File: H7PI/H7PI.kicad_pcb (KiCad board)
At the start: 4 copper layers, 65 x 30 mm, 52 parts, among them J1 XKTF-015-N, J10 DNP, J2 Header_2x10, J3 microUSB, J4 AFC07-S24ECA-00, J5 Header_2x20, J6 microUSB, J7 Header_1x2, J8 Header_1x1, J9 Header_1x1, Q1 CJ2101, Q2 CJ2102, U2 MT1470, U3 STM32H750VBT6, U4 W25Q64JVSSIQ, U5 W25Q64JVSSIQ

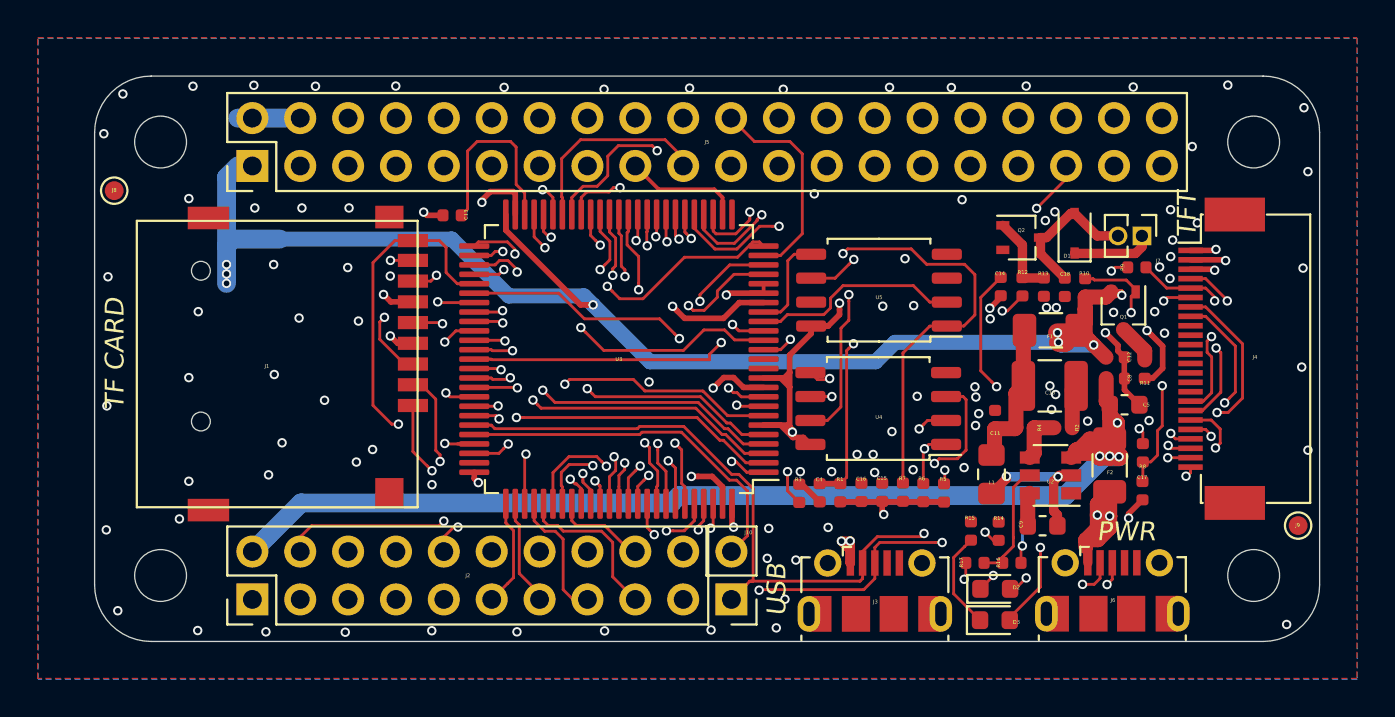
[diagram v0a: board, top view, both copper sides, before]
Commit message: v1.0开发起点 1. 不再使用树莓派外型 2. 使用Type C USB接口 3. 不再板载LCD接口 4. 板载PSRAM,QSPI FLASH,SPI FLASH 5. 保留TF卡接口
Signed-off-by: fuhua-chen <fuhua-chen@outlook.com>
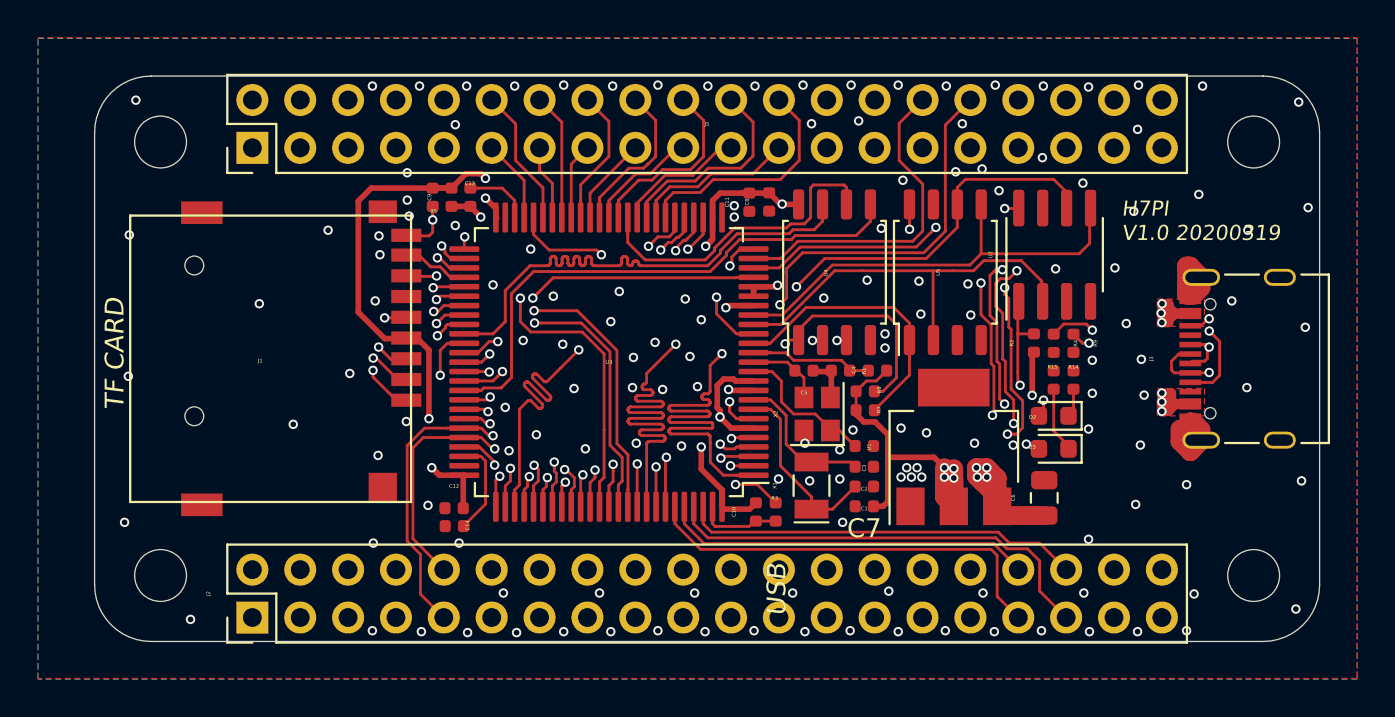
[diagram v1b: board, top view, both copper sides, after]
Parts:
- removed C15, C16, C17, C18: 100nF, C_0402_1005Metric
- removed D1: 1N5819WS, D_SOD-323
- removed F1, F2: 0458002.DR, Fuse_1206_3216Metric
- removed J10: DNP, PinHeader_1x02_P2.54mm_Vertical
- removed J4: AFC07-S24ECA-00, Connector_FPC_JS_AFC07-S24ECA-00_1x24-1MP_P0.5mm_UpSideContact
- removed J6: microUSB, USB_Micro-B_Molex-105017-0001
- removed J7: Header_1x2, Connector_PinHeader_1.27mm:PinHeader_1x02_P1.27mm_Vertical
- removed J8, J9: Header_1x1, TestPoint:TestPoint_Pad_D1.0mm
- removed L1: CIGT201610LH2R2MNE, L_0805_2012Metric_Pad1.15x1.40mm_HandSolder
- removed Q1: CJ2101, SOT-323_SC-70
- removed Q2: CJ2102, SOT-323_SC-70
- removed R10, R13, R8: 10k, R_0402_1005Metric
- removed R11: 4.7, R_0402_1005Metric
- removed R12: 1k, R_0402_1005Metric
- removed R16: 100k, R_0402_1005Metric
- removed R17: 33k, R_0402_1005Metric
- added C1: 12pF, C_0402_1005Metric, F.Cu at (170.8, 81.8)
- added C2: 12pF, C_0402_1005Metric, F.Cu at (170.8, 80.7)
- added C3: 8pF, C_0402_1005Metric, F.Cu at (170.8, 79.6)
- added C6: 22uF, Capacitor_SMD:C_0805_2012Metric, F.Cu at (180.4, 82.4)
- added C7: 10uF, C_0402_1005Metric, F.Cu at (170.8, 82.8)
- added U1: AMS1117-3.3, SOT-223, F.Cu at (175.6, 79.7)
- added X1: 32.768kHz, Crystal_SMD_EuroQuartz_EQ161-2Pin_3.2x1.5mm, F.Cu at (168.0, 81.7)
- added X2: 32MHz, Crystal:Crystal_SMD_2520-4Pin_2.5x2.0mm, F.Cu at (168.3, 77.9)
- C10: value 100uF/10V -> 100nF; footprint C_1210_3225Metric -> C_0402_1005Metric
- C5: value 1uF -> 8pF; footprint C_0603_1608Metric -> C_0402_1005Metric
- C9: value 1uF -> 100nF; footprint C_0603_1608Metric -> C_0402_1005Metric
- J2: value Header_2x10 -> Header_2x20; footprint PinHeader_2x10_P2.54mm_Vertical -> PinHeader_2x20_P2.54mm_Vertical
- J3: value microUSB -> USBC_16P_4MP; footprint USB_Micro-B_Molex-105017-0001 -> USB_C_Receptacle_Palconn_UTC16-G
- R2: value 33k -> 10k
- R4: value 100k -> 4.7k
- R9: value 10k -> 4.7k
- U2: value MT1470 -> LY68L6400SLIT; footprint SOT-23-6 -> SOIC-8_3.9x4.9mm_P1.27mm
- moved C12 36.0 mm to (149.1, 82.9), turned to 0 degrees
- moved C9 35.9 mm to (148.9, 66.4), turned to 90 degrees
- moved C14 31.7 mm to (149.1, 83.9), turned to 180 degrees
- moved R5 31.3 mm to (147.9, 66.4), turned to 90 degrees
- moved J3 22.8 mm to (190.7, 75.0), turned to 90 degrees
- moved C8 20.6 mm to (165.8, 66.7), turned to 90 degrees
- moved C11 17.4 mm to (164.7, 66.7), turned to 90 degrees
- moved C5 17.1 mm to (167.6, 75.6), turned to 180 degrees
- moved C10 17.0 mm to (165.1, 83.1), turned to 90 degrees
- moved U2 11.7 mm to (180.9, 69.5), turned to 90 degrees
- moved D2 9.69 mm to (180.9, 78.0), turned to 180 degrees
- moved D3 9.61 mm to (180.9, 79.8), turned to 180 degrees
- moved R15 9.13 mm to (180.9, 76.1)
- moved R14 8.95 mm to (181.9, 76.1)
- moved U4 7.59 mm to (169.3, 70.4), turned to 90 degrees
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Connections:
- net /TF_CDN renamed /SD_CDN
- net /TF_CMD renamed /SD_CMD
- net /TF_DATA0 renamed /SD_D0
- net /TF_DATA1 renamed /SD_D1
- net /TF_DATA2 renamed /SD_D2
- net /TF_DATA3 renamed /SD_D3
- net Net-(C4-Pad1) renamed /NRST
- C10 pad 1: Net-(C10-Pad1) -> GND
- C10 pad 2: GND -> /3V3
- C11 pad 2: Net-(C10-Pad1) -> /3V3
- C5 pad 1: /VBUS -> GND
- C5 pad 2: GND -> /OSCOUT
- C8 pad 2: /VBUS -> /3V3
- C9 pad 1: Net-(C9-Pad1) -> GND
- C9 pad 2: Net-(C9-Pad2) -> /3V3
- D2 pad 2: Net-(D2-Pad2) -> /D3
- D3 pad 2: Net-(D3-Pad2) -> /D2
- J1 pad 5: /TF_CLK -> /SD_CLK
- J2 pad 1: /3V3 -> GND
- J2 pad 10: /IO13 -> /USB_P
- J2 pad 11: /IO5 -> /D32
- J2 pad 12: /IO12 -> /D33
- J2 pad 13: /IO6 -> /D34
- J2 pad 14: /IO11 -> /D35
- J2 pad 15: /IO7 -> /D36
- J2 pad 16: /IO10 -> /D37
- J2 pad 17: /IO8 -> /D38
- J2 pad 18: /IO9 -> /D39
- J2 pad 19: GND -> /D40
- J2 pad 2: /VBUS -> GND
- J2 pad 20: GND -> /D41
- J2 pad 3: /IO1 -> GND
- J2 pad 4: /IO16 -> GND
- J2 pad 5: /IO2 -> (no net)
- J2 pad 6: /IO15 -> (no net)
- J2 pad 7: /IO3 -> (no net)
- J2 pad 8: /IO14 -> (no net)
- J2 pad 9: /IO4 -> /USB_N
- J5 pad 1: /3V3 -> GND
- J5 pad 10: /PI_RXD -> /D26
- J5 pad 11: /PI_GPIO0 -> /D25
- J5 pad 12: /PI_GPIO1 -> /D24
- J5 pad 13: /PI_GPIO2 -> /D23
- J5 pad 14: GND -> /D22
- J5 pad 15: /PI_GPIO3 -> /D21
- J5 pad 16: /PI_GPIO4 -> /D20
- J5 pad 17: /3V3 -> /D19
- J5 pad 18: /PI_GPIO5 -> /D18
- J5 pad 19: /PI_MOSI -> /D17
- J5 pad 2: /VBUS -> GND
- J5 pad 20: GND -> /D16
- J5 pad 21: /PI_MISO -> /D15
- J5 pad 22: /PI_GPIO6 -> /D14
- J5 pad 23: /PI_SCK -> /D13
- J5 pad 24: /PI_CE0 -> /D12
- J5 pad 25: GND -> /D11
- J5 pad 26: /PI_CE1 -> /D10
- J5 pad 27: /PI_SDA0 -> /D9
- J5 pad 28: /PI_SCL0 -> /D8
- J5 pad 29: /PI_GPIO21 -> /D7
- J5 pad 3: /PI_SDA1 -> GND
- J5 pad 30: GND -> /D6
- J5 pad 31: /PI_GPIO22 -> /D5
- J5 pad 32: /PI_GPIO26 -> /D4
- J5 pad 33: /PI_GPIO23 -> /D3
- J5 pad 34: GND -> /D2
- J5 pad 35: /PI_GPIO24 -> /D1
- J5 pad 36: /PI_GPIO27 -> /D0
- J5 pad 37: /PI_GPIO25 -> /3V3
- J5 pad 38: /PI_GPIO28 -> /3V3
- J5 pad 39: GND -> /VBUS
- J5 pad 4: /VBUS -> GND
- J5 pad 40: /PI_GPIO29 -> /VBUS
- J5 pad 5: /PI_SCL1 -> /D31
- J5 pad 6: GND -> /D30
- J5 pad 7: /PI_GPIO7 -> /D29
- J5 pad 8: /PI_TXD -> /D28
- J5 pad 9: GND -> /D27
- R2 pad 1: Net-(R2-Pad1) -> /3V3
- R2 pad 2: GND -> /MEM_PSRAMCS
- R3 pad 1: GND -> /BOOT0
- R3 pad 2: Net-(R3-Pad2) -> GND
- R4 pad 1: Net-(R2-Pad1) -> Net-(J3-PadB5)
- R4 pad 2: Net-(C10-Pad1) -> GND
- R7 pad 2: /FLASH_CS -> /MEM_FLASHCS
- R9 pad 1: /3V3 -> Net-(J3-PadA5)
- R9 pad 2: /TFT_CS -> GND
- U2 pad 1: GND -> /MEM_PSRAMCS
- U2 pad 2: Net-(C9-Pad2) -> /MEM_MISO
- U2 pad 3: /VBUS -> (no net)
- U2 pad 4: Net-(R2-Pad1) -> GND
- U2 pad 5: Net-(R16-Pad2) -> /MEM_MOSI
- U2 pad 6: Net-(C9-Pad1) -> /MEM_SCK
- U3 pad 12: (no net) -> /OSCIN
- U3 pad 13: (no net) -> /OSCOUT
- U3 pad 15: /PI_GPIO5 -> /MEM_FLASHCS
- U3 pad 16: /TF_CLK -> /D4
- U3 pad 17: /FLASH_MISO -> /MEM_MISO
- U3 pad 18: /FLASH_MOSI -> /MEM_MOSI
- U3 pad 2: /PI_GPIO0 -> /D0
- U3 pad 23: /QSPI_IO3 -> /D5
- U3 pad 24: /PI_GPIO6 -> /D6
- U3 pad 25: /PI_GPIO7 -> /D7
- U3 pad 28: /PI_GPIO21 -> /D8
- U3 pad 29: /PI_GPIO22 -> /D9
- U3 pad 3: /PI_GPIO1 -> /D1
- U3 pad 30: /PI_GPIO23 -> /D10
- U3 pad 31: /PI_GPIO24 -> /D11
- U3 pad 32: /PI_GPIO25 -> /D12
- U3 pad 33: /PI_GPIO26 -> /D13
- U3 pad 34: /PI_GPIO27 -> /D14
- U3 pad 35: /PI_GPIO28 -> /D15
- U3 pad 37: /TFT_DB12 -> /D16
- U3 pad 38: /TFT_DB13 -> /D17
- U3 pad 39: /TFT_DB14 -> /D18
- U3 pad 4: /PI_GPIO2 -> /D2
- U3 pad 40: /TFT_DB15 -> /D19
- U3 pad 41: /PI_CE0 -> /D20
- U3 pad 42: /PI_SCK -> /D21
- U3 pad 43: /PI_MISO -> /D22
- U3 pad 44: /PI_MOSI -> /D23
- U3 pad 45: /PI_CE1 -> /D24
- U3 pad 46: /PI_SCL1 -> /MEM_SCK
- U3 pad 47: /PI_SDA1 -> /D25
- U3 pad 5: /PI_GPIO3 -> /D3
- U3 pad 51: /FLASH_CS -> /D26
- U3 pad 52: /FLASH_SCK -> /D27
- U3 pad 56: /PI_GPIO29 -> /D28
- U3 pad 57: /IO1 -> /D29
- U3 pad 58: /TFT_RS -> /D30
- U3 pad 59: /BUZZER -> /D31
- U3 pad 60: /IO2 -> /QSPI_IO3
- U3 pad 61: /TFT_DB8 -> /D32
- U3 pad 62: /TFT_DB9 -> /D33
- U3 pad 63: /TFT_BL -> /D34
- U3 pad 64: /TFT_CS -> /D35
- U3 pad 65: /TFT_RST -> /D36
- U3 pad 67: /IO3 -> /D37
- U3 pad 68: /PI_TXD -> /D38
- U3 pad 69: /PI_RXD -> /D39
- U3 pad 7: /PI_GPIO4 -> /MEM_PSRAMCS
- U3 pad 72: /IO4 -> /D40
- U3 pad 76: /IO5 -> /D41
- U3 pad 77: /IO6 -> /D42
- U3 pad 79: /IO7 -> /D43
- U3 pad 8: Net-(D2-Pad2) -> /OSC32IN
- U3 pad 80: /IO8 -> /D44
- U3 pad 81: /TFT_DB10 -> /D45
- U3 pad 82: /TFT_DB11 -> /D46
- U3 pad 83: /IO9 -> /D47
- U3 pad 84: /IO10 -> /D48
- U3 pad 85: /TFT_RD -> /D49
- U3 pad 86: /TFT_WR -> /D50
- U3 pad 87: /IO11 -> /SD_CLK
- U3 pad 88: /IO12 -> /D51
- U3 pad 9: Net-(D3-Pad2) -> /OSC32OUT
- U3 pad 91: /IO13 -> /D52
- U3 pad 93: /PI_SDA0 -> /D53
- U3 pad 94: Net-(R3-Pad2) -> /BOOT0
- U3 pad 95: /PI_SCL0 -> /D54
- U3 pad 96: /IO14 -> /D55
- U3 pad 97: /IO15 -> /D56
- U3 pad 98: /IO16 -> /D57
- U5 pad 1: /FLASH_CS -> /MEM_FLASHCS
- U5 pad 2: /FLASH_MISO -> /MEM_MISO
- U5 pad 5: /FLASH_MOSI -> /MEM_MOSI
- U5 pad 6: /FLASH_SCK -> /MEM_SCK
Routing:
- net /TFT_RST: track 53.0 -> 0.00 mm, vias 3 -> 0
- net /3V3: track 237.0 -> 184.5 mm, vias 19 -> 16
- net /TFT_DB15: track 49.1 -> 0.00 mm, vias 3 -> 0
- net /PI_GPIO29: track 48.4 -> 0.00 mm, vias 2 -> 0
- net /TFT_CS: track 48.2 -> 0.00 mm, vias 2 -> 0
- net /TFT_RD: track 48.1 -> 0.00 mm, vias 2 -> 0
- net /TFT_WR: track 47.3 -> 0.00 mm, vias 2 -> 0
- net /TFT_DB14: track 47.2 -> 0.00 mm, vias 3 -> 0
- net /TFT_DB13: track 45.1 -> 0.00 mm, vias 3 -> 0
- net /TFT_DB9: track 44.5 -> 0.00 mm, vias 2 -> 0
- net /TFT_DB8: track 44.5 -> 0.00 mm, vias 2 -> 0
- net /TFT_DB12: track 42.7 -> 0.00 mm, vias 3 -> 0
- net /FLASH_CS: track 42.4 -> 0.00 mm, vias 2 -> 0
- net /D2: track 0.00 -> 42.3 mm, vias 0 -> 4
- net /SD_CDN: track 50.5 -> 8.21 mm
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- added copper zone on F.Cu, net /VBUS
- added copper zone on In1.Cu, net GND
- added copper zone on In2.Cu, net GND
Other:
- board text added: "H7PI V1.0 20200319"
- board text removed: "H7PI ZERO V0.3 20191228"
- board text removed: "PWR"
- board text removed: "TFT"
